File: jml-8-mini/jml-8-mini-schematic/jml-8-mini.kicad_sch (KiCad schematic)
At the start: 6 parts, among them J6 Z80 Lines, U1 Z80CPU

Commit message: add to info section of schematic
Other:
- company: (none) -> https://github.com/jac-oblong/jml
- title: jml-8 mini schematic -> JML-8 Mini Schematic
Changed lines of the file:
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@@
   (paper "A4")
   (title_block
-    (title "jml-8 mini schematic")
+    (title "JML-8 Mini Schematic")
     (date "2023-10-02")
     (rev "A")
-    (comment 1 "Author: Jacob Long")
+    (company "https://github.com/jac-oblong/jml")
+    (comment 1 "Design of Z80 based microcomputer")
+    (comment 3 "Released under MIT License")
+    (comment 4 "Created by: Jacob Long (https://github.com/jac-oblong)")
   )
   (junction (at 149.86 147.955) (diameter 0) (color 0 0 0 0)

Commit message: update info section of schematic
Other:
- company: https://github.com/jac-oblong/jml -> https://github.com/jac-oblong/JML
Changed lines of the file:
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@@
     (date "2023-10-02")
     (rev "A")
-    (company "https://github.com/jac-oblong/jml")
+    (company "https://github.com/jac-oblong/JML")
     (comment 1 "Design of Z80 based microcomputer")
     (comment 3 "Released under MIT License")

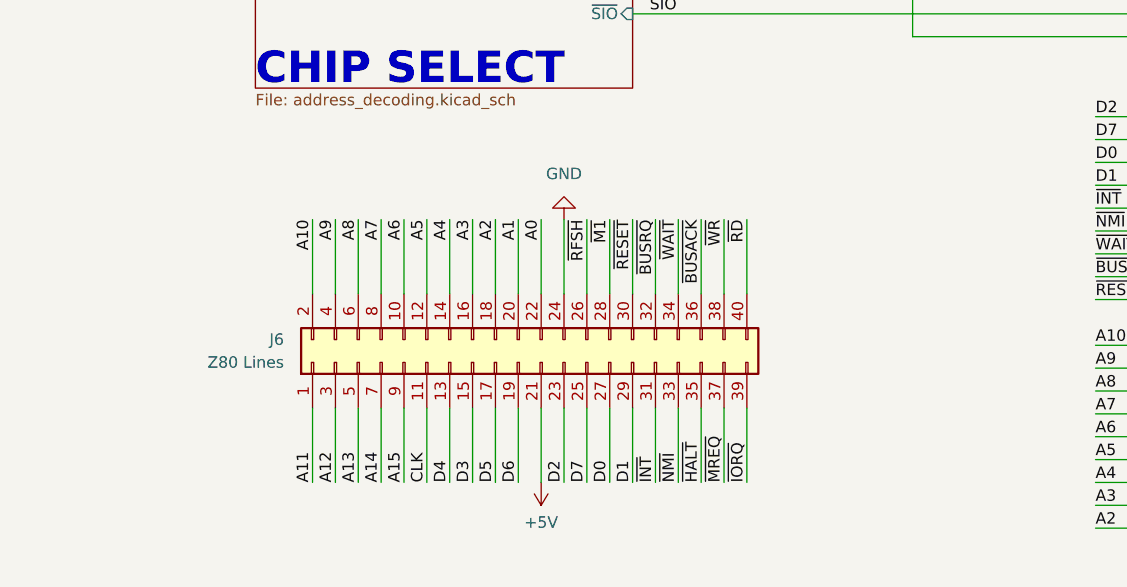
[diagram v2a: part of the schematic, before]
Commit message: add mounting holes for PCB
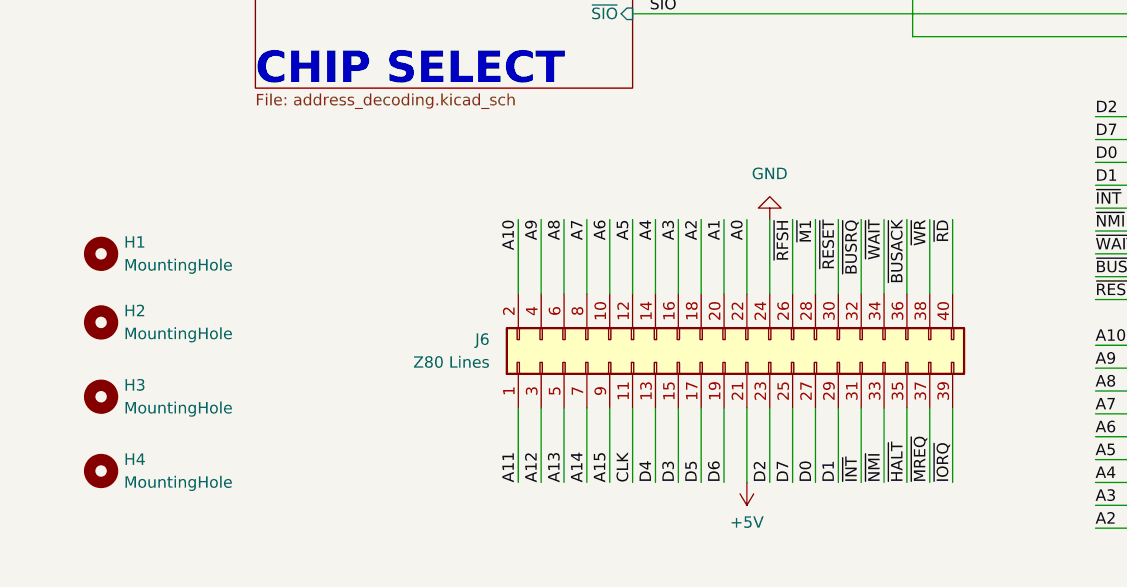
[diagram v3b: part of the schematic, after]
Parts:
- added H1, H2, H3, H4: MountingHole, MountingHole:MountingHole_5mm, symbol Mechanical:MountingHole
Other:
- moved on the sheet: J6

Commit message: change more footprints
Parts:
- U1: footprint Package_DIP:DIP-40_W15.24mm_LongPads -> Package_DIP:DIP-40_W15.24mm_Socket_LongPads
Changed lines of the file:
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@@
       (effects (font (size 1.27 1.27)) (justify left))
     )
-    (property "Footprint" "Package_DIP:DIP-40_W15.24mm_LongPads" (at 149.86 71.755 0)
+    (property "Footprint" "Package_DIP:DIP-40_W15.24mm_Socket_LongPads" (at 149.86 71.755 0)
       (effects (font (size 1.27 1.27)) hide)
     )

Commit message: swap pins on resistor network for easier pcb connection
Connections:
- net ~{RESET}: now also RN1.8 (R7); no longer RN1.10 (R9)
- net ~{WAIT}: now also RN1.10 (R9); no longer RN1.8 (R7)
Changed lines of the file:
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@@
     (effects (font (size 1.27 1.27)) (justify right bottom))
   )
-  (label "~{RESET}" (at 129.54 168.275 0) (fields_autoplaced)
+  (label "~{RESET}" (at 129.54 163.195 0) (fields_autoplaced)
     (effects (font (size 1.27 1.27)) (justify left bottom))
   )
@@
     (effects (font (size 1.27 1.27)) (justify left bottom))
   )
-  (label "~{WAIT}" (at 129.54 163.195 0) (fields_autoplaced)
-    (effects (font (size 1.27 1.27)) (justify left bottom))
-  )
+  (label "~{WAIT}" (at 129.54 168.275 0) (fields_autoplaced)
+    (effects (font (size 1.27 1.27)) (justify left bottom))
+  )

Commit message: lots of updates to schematic to make pcb routing easier, start on pcb design
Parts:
- added H5: MountingHole, MountingHole:MountingHole_3.2mm_M3, symbol Mechanical:MountingHole
- H1, H2, H3, H4: footprint MountingHole:MountingHole_5mm -> MountingHole:MountingHole_3.2mm_M3
- RN1, RN2, RN3, RN4: value 10k -> 10K
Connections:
- net A0: now also RN4.8 (R7); no longer RN4.3 (R2)
- net A1: now also RN4.9 (R8); no longer RN4.2 (R1)
- net A10: now also RN3.10 (R9); no longer RN3.2 (R1)
- net A2: now also RN3.2 (R1); no longer RN3.10 (R9)
- net A3: now also RN3.3 (R2); no longer RN3.9 (R8)
- net A4: now also RN3.4 (R3); no longer RN3.8 (R7)
- net A5: now also RN3.5 (R4); no longer RN3.7 (R6)
- net A7: now also RN3.7 (R6); no longer RN3.5 (R4)
- net A8: now also RN3.8 (R7); no longer RN3.4 (R3)
- net A9: now also RN3.9 (R8); no longer RN3.3 (R2)
- net ~{CTC}: now also RN4.6 (R5); no longer RN4.9 (R8)
- net ~{RAM}: now also RN4.4 (R3); no longer RN4.8 (R7)
- net ~{ROM WE}: now also RN4.2 (R1); no longer RN4.6 (R5)
- net ~{ROM}: now also RN4.3 (R2); no longer RN4.7 (R6)
- net ~{SIO SYNCA}: now also RN4.7 (R6); no longer RN4.4 (R3)
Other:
- note added: "Mounting"
- note added: "Pull Up Resistors"
- note added: "Z80 Breakout"
- moved on the sheet: H1, H2, H3, J6, RN1, RN2, RN3, RN4

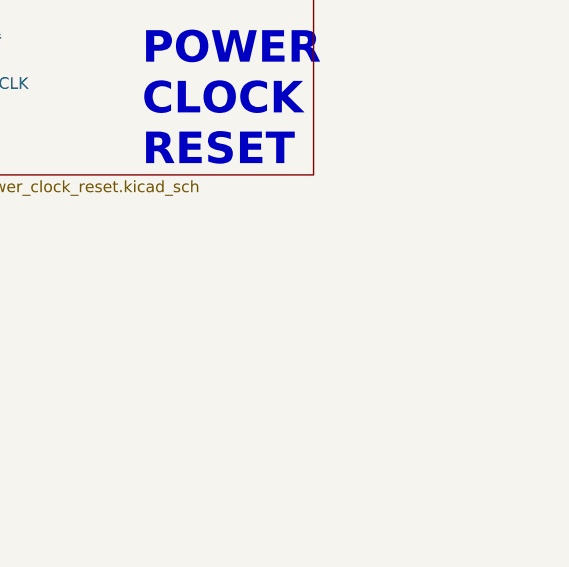
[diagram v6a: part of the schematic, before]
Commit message: fix wrong label, add labels and figures to pcb
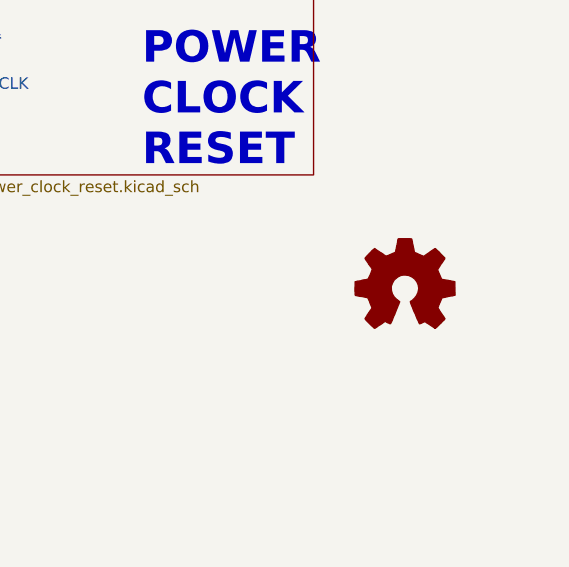
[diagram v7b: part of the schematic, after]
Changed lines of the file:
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@@
+    )
+  )
+  (symbol (lib_id "Graphic:Logo_Open_Hardware_Small") (at 270.51 157.48 0) (unit 1)
+    (in_bom no) (on_board no) (dnp no) (fields_autoplaced)
+    (property "Reference" "#SYM1" (at 270.51 150.495 0)
+      (effects (font (size 1.27 1.27)) hide)
+    )
+    (property "Value" "Logo_Open_Hardware_Small" (at 270.51 163.195 0)
+      (effects (font (size 1.27 1.27)) hide)
+    )
+    (property "Footprint" "" (at 270.51 157.48 0)
+      (effects (font (size 1.27 1.27)) hide)
+    )
+    (property "Datasheet" "~" (at 270.51 157.48 0)
+      (effects (font (size 1.27 1.27)) hide)
+    )
+    (property "Sim.Enable" "0" (at 270.51 157.48 0)
+      (effects (font (size 1.27 1.27)) hide)
+    )
+    (instances
+      (project "jml-8-mini"
+        (path "/7f93abb4-2372-4a9e-a664-5edb67349db4"
+          (reference "#SYM1") (unit 1)
+        )
+      )
     )
   )

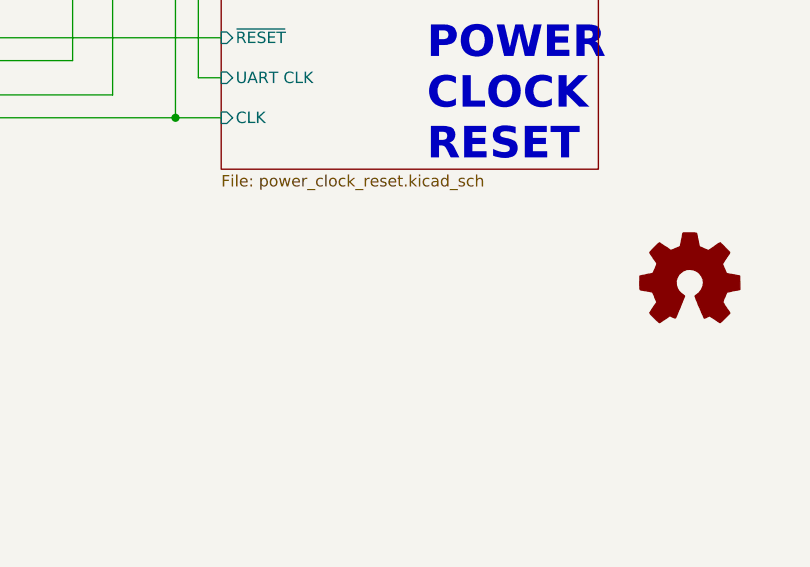
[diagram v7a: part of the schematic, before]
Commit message: new symbol & footprint for logo, add to schematic and pcb
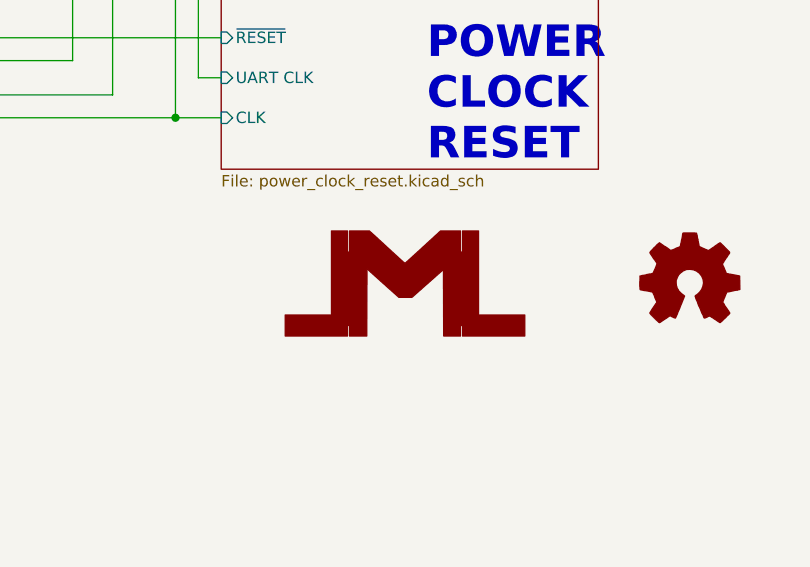
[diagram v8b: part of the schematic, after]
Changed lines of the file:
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@@
+    )
+  )
+  (symbol (lib_id "jml-8-mini-library:JML_Logo") (at 240.03 157.48 0) (unit 1)
+    (in_bom yes) (on_board yes) (dnp no) (fields_autoplaced)
+    (property "Reference" "#G1" (at 240.03 152.2786 0)
+      (effects (font (size 1.27 1.27)) hide)
+    )
+    (property "Value" "JML_Logo" (at 240.03 162.6814 0)
+      (effects (font (size 1.27 1.27)) hide)
+    )
+    (property "Footprint" "" (at 240.03 157.48 0)
+      (effects (font (size 1.27 1.27)) hide)
+    )
+    (property "Datasheet" "" (at 240.03 157.48 0)
+      (effects (font (size 1.27 1.27)) hide)
+    )
+    (instances
+      (project "jml-8-mini"
+        (path "/7f93abb4-2372-4a9e-a664-5edb67349db4"
+          (reference "#G1") (unit 1)
+        )
+      )
     )
   )
